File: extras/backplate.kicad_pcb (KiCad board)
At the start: 2 copper layers, 344.4 x 130.9 mm, 7 parts

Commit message: update plate and add feet to bottom
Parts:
- added REF**: feet, custom_parts:feet, F.Cu at (368.3, 91.4)
- added REF**: feet, custom_parts:feet, F.Cu at (58.4, 91.4)

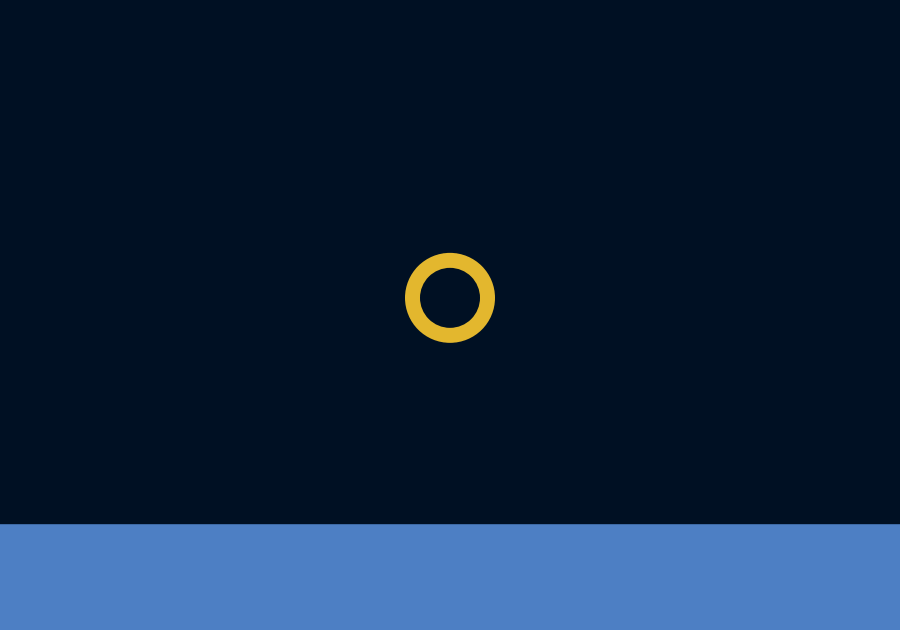
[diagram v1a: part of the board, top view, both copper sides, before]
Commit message: fix screwhole position on backplate
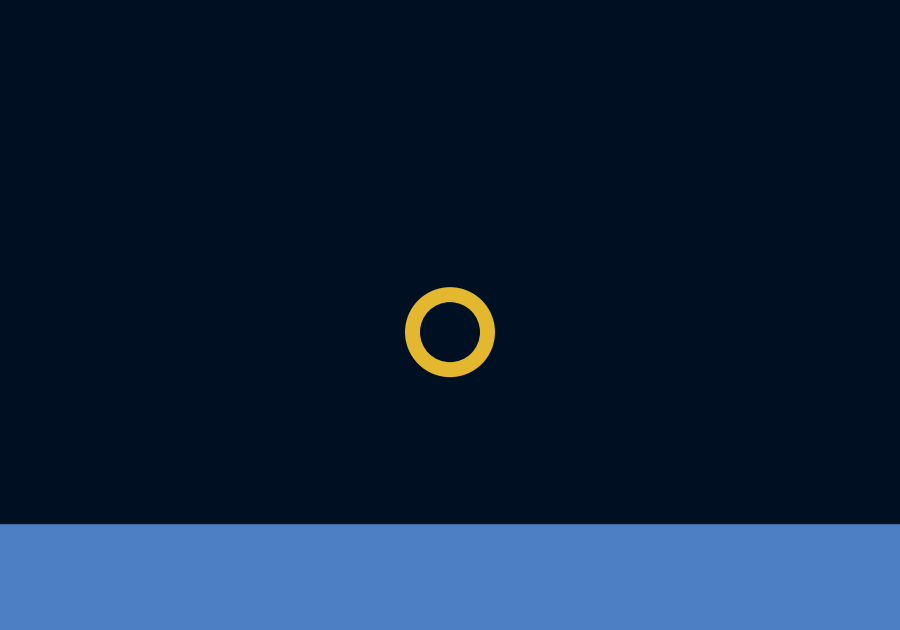
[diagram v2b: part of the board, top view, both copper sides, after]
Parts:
- moved REF** 1.14 mm to (211.8, 77.2)

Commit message: update gerbers to latest kicad version defaults
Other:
- rule pad_to_mask_clearance: 0.05 -> 0
